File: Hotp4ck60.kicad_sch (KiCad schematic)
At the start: 50 parts, among them J1 HRO_TYPE-C-31-M-12, SW44 RST, U1 nRF52840, U2 SRV05-4, Y1 32 MHz, Y2 32.768 Khz

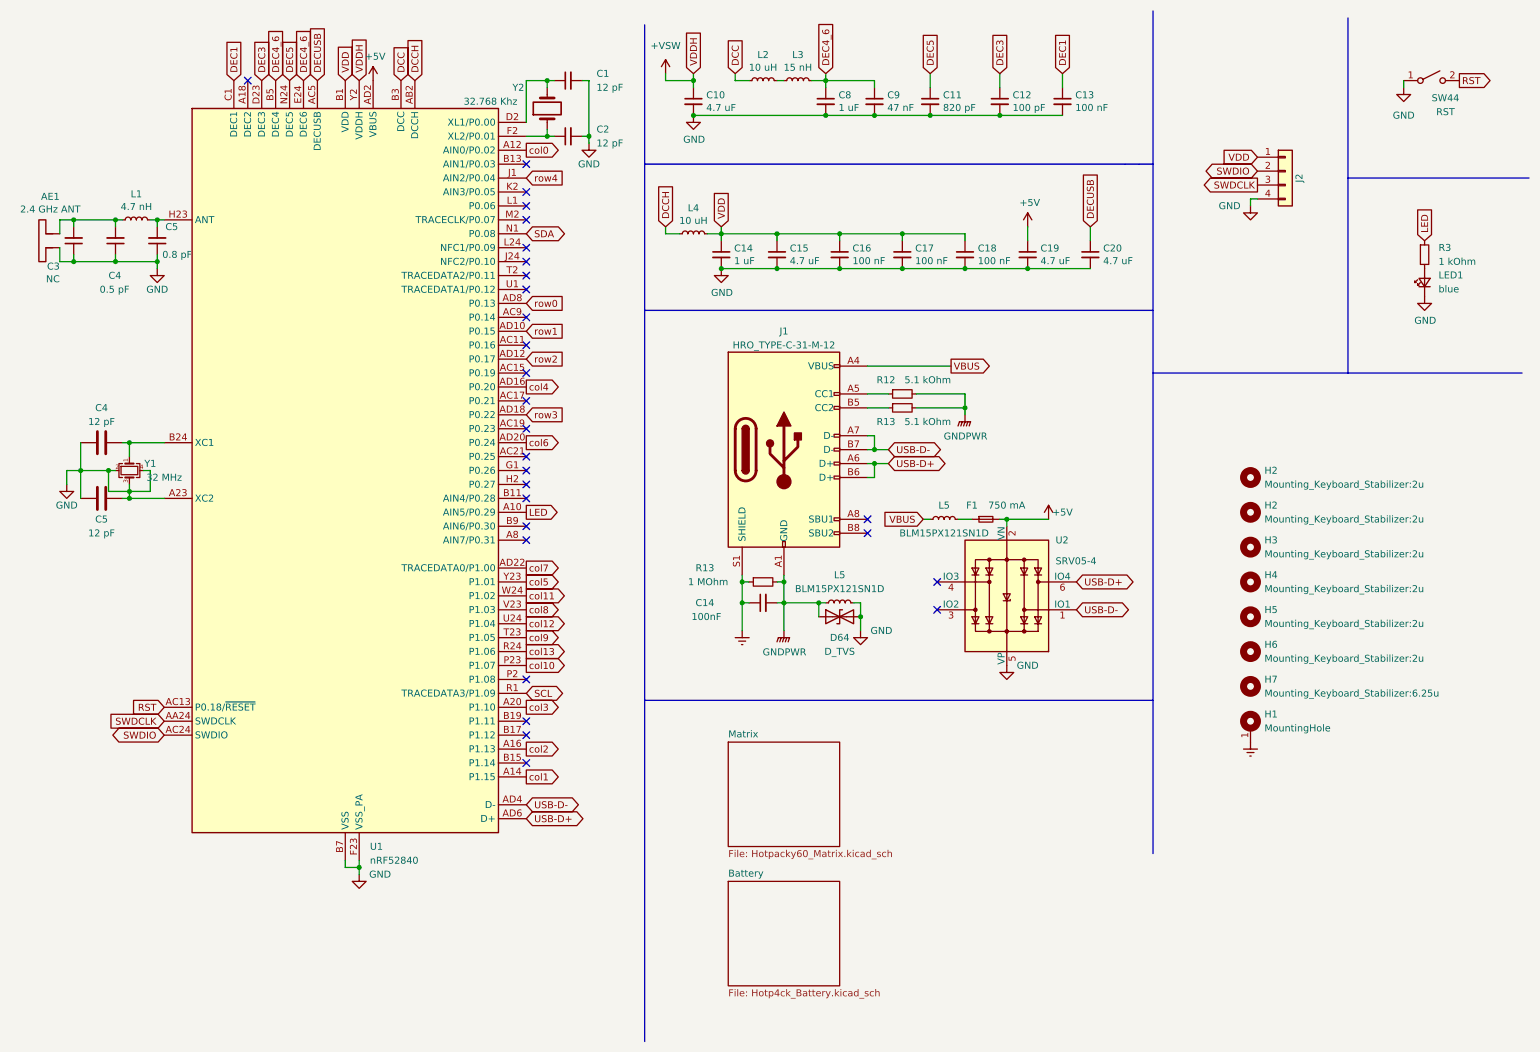
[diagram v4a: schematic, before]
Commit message: Add Switch Mount pin symbol
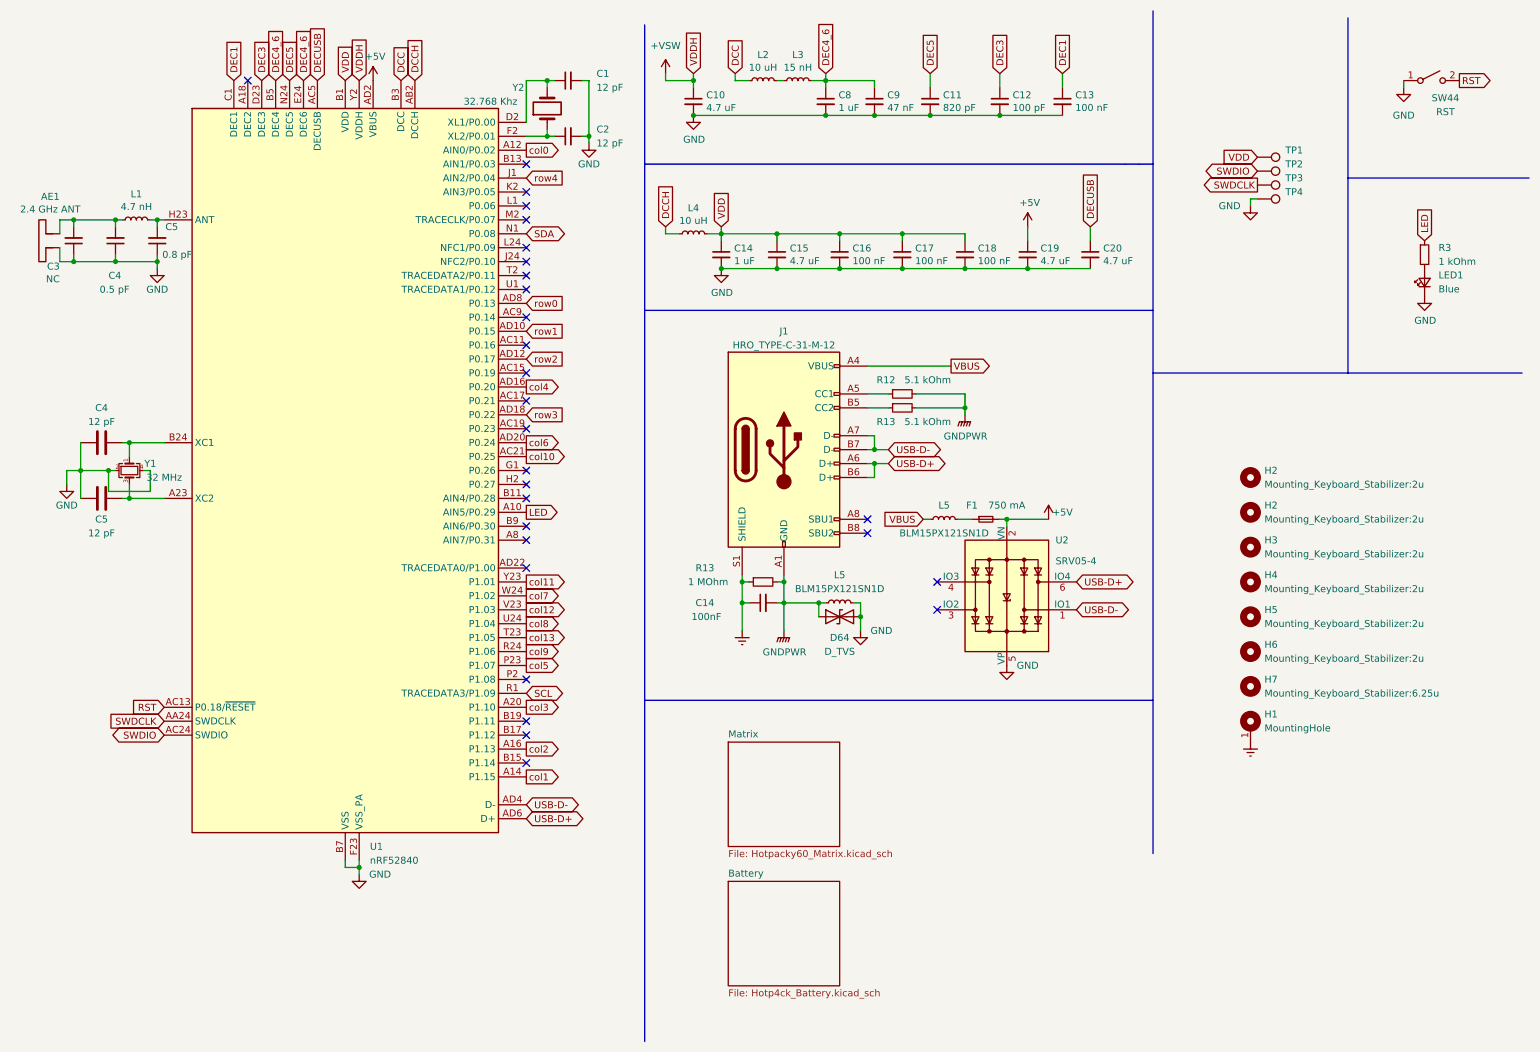
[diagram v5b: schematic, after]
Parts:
- removed J2: ~, Connector_PinSocket_2.54mm:PinSocket_1x04_P2.54mm_Vertical, symbol Connector_Generic:Conn_01x04
- added TP1: TestPoint, TestPoint:TestPoint_THTPad_1.0x1.0mm_Drill0.5mm, symbol Connector:TestPoint
- added TP2, TP3, TP4: TestPoint, TestPoint:TestPoint_THTPad_D1.0mm_Drill0.5mm, symbol Connector:TestPoint
- LED1: value blue -> Blue
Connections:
- net GND: now also TP4.1; no longer C5.1, U1.A23 (XC2), Y1.3
- net SWDCLK: now also TP3.1
- net SWDIO: now also TP2.1
- net VDD: now also TP1.1
- net col10: now also U1.AC21 (P0.25); no longer U1.P23 (P1.07)
- net col11: now also U1.Y23 (P1.01); no longer U1.W24 (P1.02)
- net col12: now also U1.V23 (P1.03); no longer U1.U24 (P1.04)
- net col13: now also U1.T23 (P1.05); no longer U1.R24 (P1.06)
- net col5: now also U1.P23 (P1.07); no longer U1.Y23 (P1.01)
- net col7: now also U1.W24 (P1.02); no longer U1.AD22 (TRACEDATA0/P1.00)
- net col8: now also U1.U24 (P1.04); no longer U1.V23 (P1.03)
- net col9: now also U1.R24 (P1.06); no longer U1.T23 (P1.05)
- new net: C5.1, U1.A23 (XC2), Y1.3
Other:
- moved on the sheet: C5

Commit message: Change schematic
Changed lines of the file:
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@@
     (stroke (width 0) (type solid))
+  )
+  (wire (pts (xy 74.93 21.59) (xy 74.93 24.13))
+    (stroke (width 0) (type default))
   )
   (wire (pts (xy 69.85 167.64) (xy 72.39 167.64))
@@
     )
   )
-  (global_label "VDDH" (shape input) (at 72.39 24.13 90) (fields_autoplaced)
-    (effects (font (size 1.27 1.27)) (justify left))
-    (property "Intersheetrefs" "${INTERSHEET_REFS}" (at -15.24 -107.95 0)
-      (effects (font (size 1.27 1.27)) hide)
-    )
-  )
   (global_label "VDDH" (shape input) (at 133.35 22.86 90) (fields_autoplaced)
     (effects (font (size 1.27 1.27)) (justify left))
@@
     )
   )
+  (global_label "VDDH" (shape input) (at 72.39 24.13 90) (fields_autoplaced)
+    (effects (font (size 1.27 1.27)) (justify left))
+    (property "Intersheetrefs" "${INTERSHEET_REFS}" (at -82.55 -204.47 0)
+      (effects (font (size 1.27 1.27)) hide)
+    )
+  )
   (global_label "DEC3" (shape input) (at 189.23 22.86 90) (fields_autoplaced)
     (effects (font (size 1.27 1.27)) (justify left))
@@
       (project "Hotp4ck60"
         (path "/a57939d7-40ce-4436-8014-db245ef7f3c5"
-          (reference "R14") (unit 1)
+          (reference "R3") (unit 1)
         )
       )
@@
   (symbol (lib_id "Device:R_Small") (at 266.7 55.88 0) (unit 1)
     (in_bom yes) (on_board yes) (dnp no) (fields_autoplaced)
-    (property "Reference" "R3" (at 269.24 54.6099 0)
-      (effects (font (size 1.27 1.27)) (justify left))
-    )
-    (property "Value" "1 kOhm" (at 269.24 57.1499 0)
+    (property "Reference" "R3" (at 269.24 54.61 0)
+      (effects (font (size 1.27 1.27)) (justify left))
+    )
+    (property "Value" "1 kOhm" (at 269.24 57.15 0)
       (effects (font (size 1.27 1.27)) (justify left))
     )
@@
       (project "Hotp4ck60"
         (path "/a57939d7-40ce-4436-8014-db245ef7f3c5"
-          (reference "R5") (unit 1)
+          (reference "R4") (unit 1)
         )
       )
@@
     )
   )
-  (symbol (lib_id "power:+5V") (at 74.93 24.13 0) (unit 1)
-    (in_bom yes) (on_board yes) (dnp no)
-    (property "Reference" "#PWR01" (at 74.93 27.94 0)
-      (effects (font (size 1.27 1.27)) hide)
-    )
-    (property "Value" "+5V" (at 75.311 19.7358 0)
-      (effects (font (size 1.27 1.27)))
-    )
-    (property "Footprint" "" (at 74.93 24.13 0)
-      (effects (font (size 1.27 1.27)) hide)
-    )
-    (property "Datasheet" "" (at 74.93 24.13 0)
-      (effects (font (size 1.27 1.27)) hide)
-    )
+  (symbol (lib_id "power:+5V") (at 74.93 21.59 0) (unit 1)
+    (in_bom yes) (on_board yes) (dnp no)
+    (property "Reference" "#PWR01" (at 74.93 25.4 0)
+      (effects (font (size 1.27 1.27)) hide)
+    )
+    (property "Value" "+5V" (at 76.2 17.78 0)
+      (effects (font (size 1.27 1.27)))
+    )
+    (property "Footprint" "" (at 74.93 21.59 0)
+      (effects (font (size 1.27 1.27)) hide)
+    )
+    (property "Datasheet" "" (at 74.93 21.59 0)
+      (effects (font (size 1.27 1.27)) hide)
+    )

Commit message: Update
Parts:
- C14: value 100nF -> 100 nF
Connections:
- net LED: now also U1.A8 (AIN7/P0.31); no longer U1.A10 (AIN5/P0.29)
- net RST: now also U1.AD12 (P0.17)
- net SCL: now also U1.AD8 (P0.13); no longer U1.R1 (TRACEDATA3/P1.09)
- net SDA: now also U1.AD10 (P0.15); no longer U1.N1 (P0.08)
- net col10: now also U1.R24 (P1.06); no longer U1.AC21 (P0.25)
- net col11: now also U1.U24 (P1.04); no longer U1.Y23 (P1.01)
- net col12: now also U1.W24 (P1.02); no longer U1.V23 (P1.03)
- net col13: now also U1.AC21 (P0.25), U1.AD22 (TRACEDATA0/P1.00); no longer U1.T23 (P1.05)
- net col4: now also U1.J1 (AIN2/P0.04); no longer U1.AD16 (P0.20)
- net col5: now also U1.AD16 (P0.20); no longer U1.P23 (P1.07)
- net col6: now also U1.J24 (NFC2/P0.10); no longer U1.AD20 (P0.24)
- net col7: now also U1.AD18 (P0.22); no longer U1.W24 (P1.02)
- net col8: now also U1.L24 (NFC1/P0.09); no longer U1.U24 (P1.04)
- net col9: now also U1.AD20 (P0.24); no longer U1.R24 (P1.06)
- net row0: now also U1.R1 (TRACEDATA3/P1.09); no longer U1.AD8 (P0.13)
- net row1: now also U1.N1 (P0.08); no longer U1.AD10 (P0.15)
- net row2: now also U1.L1 (P0.06); no longer U1.AD12 (P0.17)
- net row3: now also U1.A10 (AIN5/P0.29); no longer U1.AD18 (P0.22)
- net row4: now also U1.U1 (TRACEDATA1/P0.12); no longer U1.J1 (AIN2/P0.04)
- no-connect marks 28 -> 26

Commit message: Make Readme.md
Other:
- moved on the sheet: C10, C11, C12, C13, C8, C9, L2, L3
